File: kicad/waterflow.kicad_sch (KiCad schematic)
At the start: 14 parts, among them J1 Terminal, Q1 BC547, Q2 BC547, Q3 AO4447, U1 WeMos_D1_mini

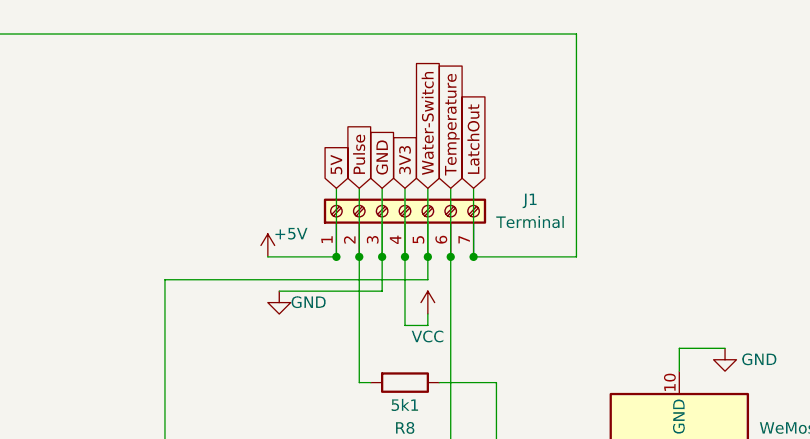
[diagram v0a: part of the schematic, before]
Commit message: changed: label 3V3 -> VCC
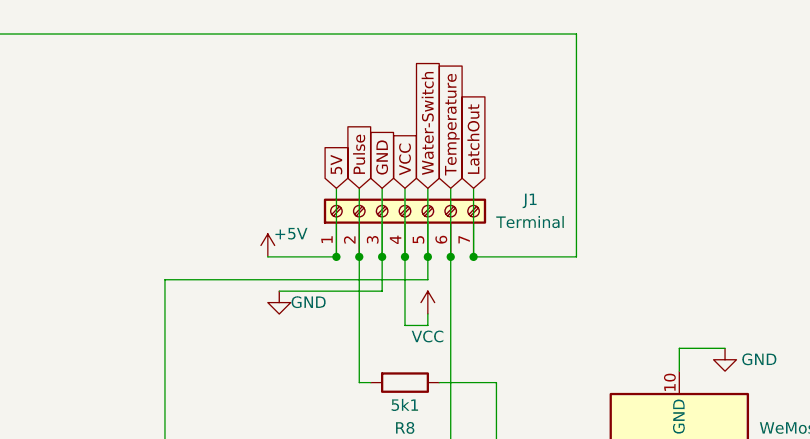
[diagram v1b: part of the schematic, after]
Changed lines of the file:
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@@
     )
   )
-  (global_label "3V3" (shape input) (at 180.34 44.45 90) (fields_autoplaced)
+  (global_label "VCC" (shape input) (at 180.34 44.45 90) (fields_autoplaced)
     (effects (font (size 1.27 1.27)) (justify left))
-    (property "Intersheet References" "${INTERSHEET_REFS}" (id 0) (at 180.2606 38.5293 90)
+    (property "Intersheet References" "${INTERSHEET_REFS}" (id 0) (at 180.2606 38.4083 90)
       (effects (font (size 1.27 1.27)) (justify left) hide)
     )

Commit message: release v1.1
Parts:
- added R3: 22K, Resistor_THT:R_Axial_DIN0207_L6.3mm_D2.5mm_P10.16mm_Horizontal, symbol Device:R
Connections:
- net LatchOut: now also J1.6 (Pin_6); no longer J1.7 (Pin_7)
- net Temperature: now also J1.7 (Pin_7), R3.1; no longer J1.6 (Pin_6)
- net at U1.13 (SDA/D2): now also R5.1
- net at U1.3 (D0): now also R3.2
- net at U1.7 (CS/D8): no longer R5.1
